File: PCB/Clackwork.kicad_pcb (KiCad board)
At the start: 2 copper layers, 100 x 69.5 mm, 26 parts, among them J1 Conn_01x08_Pin, SW1 SW_Push_45deg, SW2 SW_Push_45deg, SW3 SW_Push_45deg, SW4 SW_Push_45deg, SW5 SW_Push_45deg, SW6 SW_Push_45deg, SW7 SW_Push_45deg, SW8 SW_Push_45deg, U1 XIAO-ESP32-C3-SMD

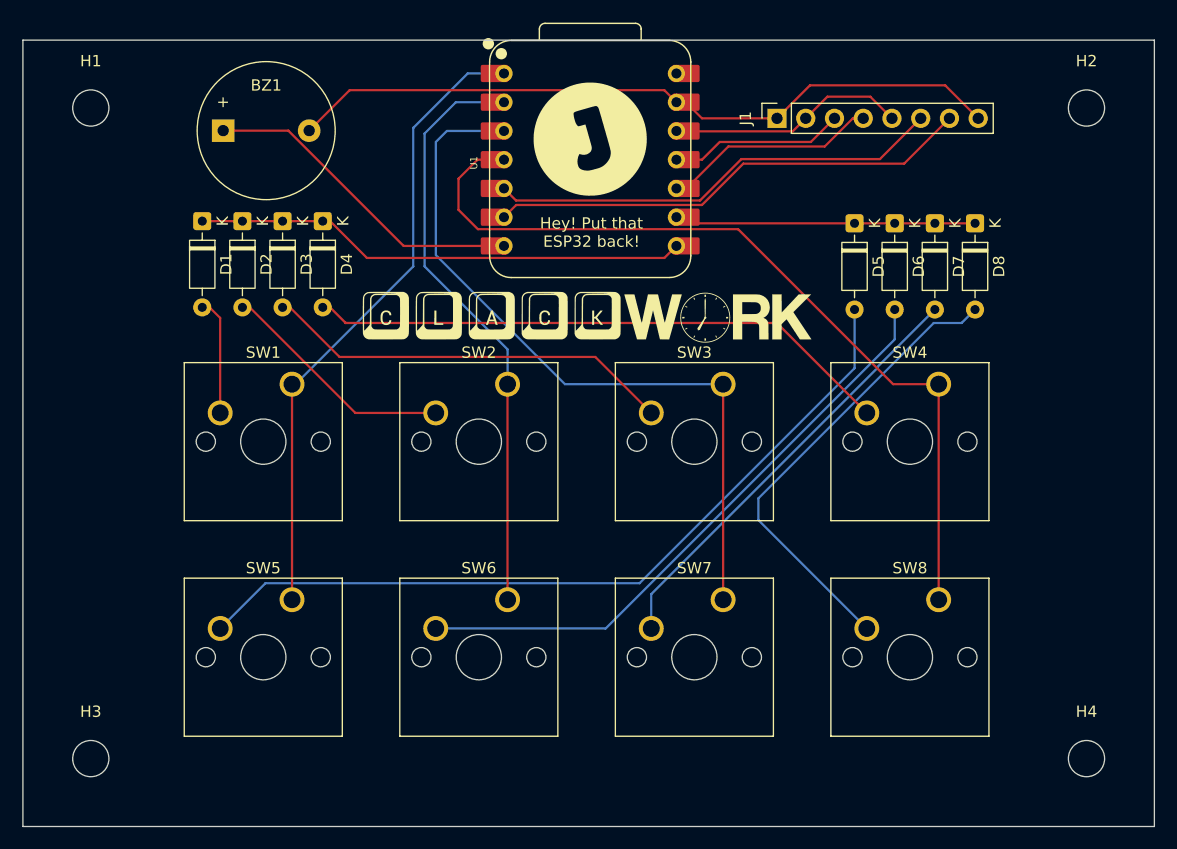
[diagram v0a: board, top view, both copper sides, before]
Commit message: Added finished CAD files
- Removed old 3d model STEP files from the CAD folder
- Added the completed case model files
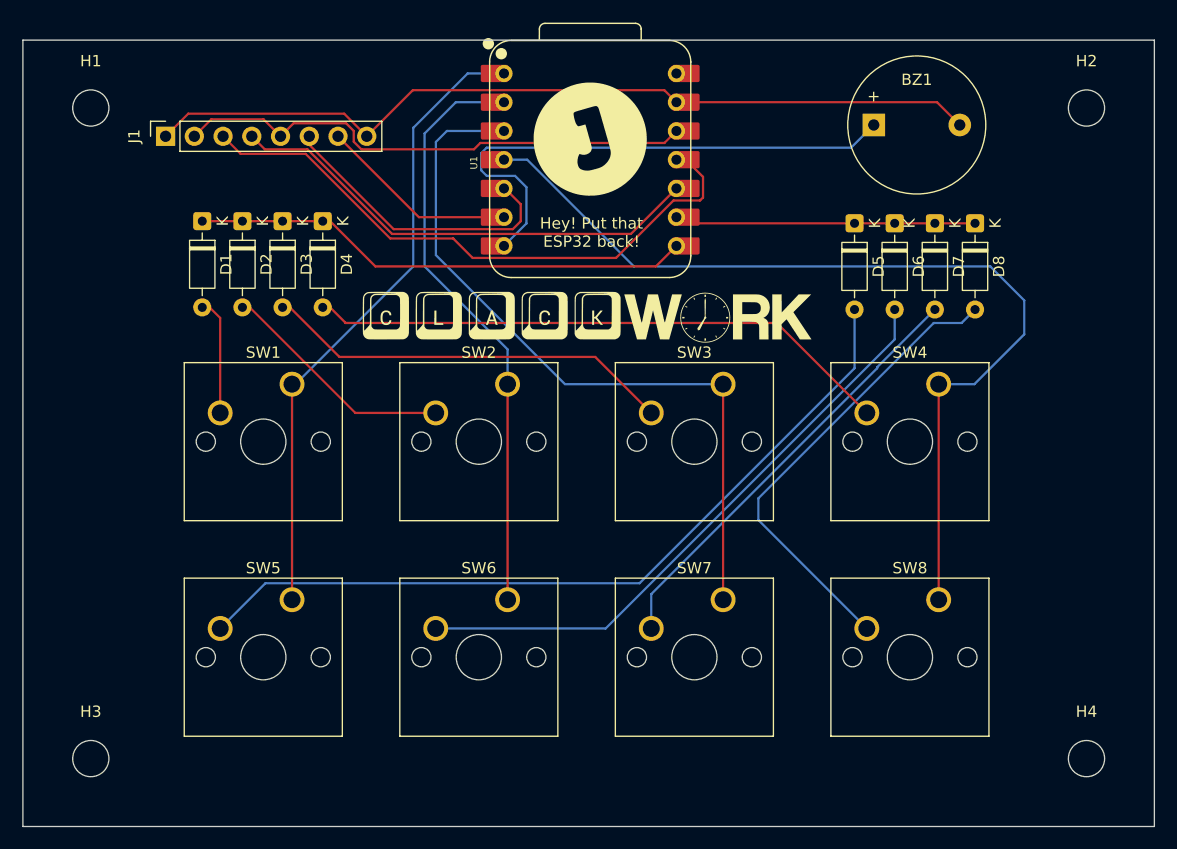
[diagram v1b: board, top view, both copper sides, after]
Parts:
- moved BZ1 57.5 mm to (172.7, 62.5)
- moved J1 54.1 mm to (110.1, 63.5)
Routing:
- net /SDA: track 14.6 -> 53.1 mm
- net +3.3V: track 20.3 -> 46.6 mm
- net /CS: track 43.0 -> 16.8 mm
- net /SCL: track 18.2 -> 43.7 mm
- net Net-(BZ1-+): track 28.2 -> 47.9 mm
- net /DC: track 40.3 -> 26.4 mm
- net GND: track 63.2 -> 74.0 mm
- net COL3: track 74.5 -> 82.6 mm
- net ROW0: track 43.0 -> 43.7 mm
